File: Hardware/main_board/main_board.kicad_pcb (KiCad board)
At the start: 6 copper layers, 95.4 x 36.1 mm, 282 parts, among them J1 BATT, J2 LCD, J3 BACK_LIGHT, J4 SD, J5 NFC, J6 EXT1, J7 EXT0, J8 USB_C, Q1 DMN313DLT, SW1 OK, SW2 BACK, SW3 RIGHT, SW4 LEFT, SW5 UP, SW6 DOWN, T1 B0310J50100AHF, U1 STM32WB55RGVx, U10 BGS13S4N9E6327XTSA1, U11 NC7SZ32M5X, U12 LP5562TMX, U2 BQ27220YZFR, U3 BQ25896RTWR, U4 RS3221-3.3YF3, U5 LM66100DCK, U6 LM3281YFQR, U7 LM3281YFQR, U8 CC1101RGP, U9 BGS13S4N9E6327XTSA1, Y1 32MHz, Y2 32.768K, Y3 26MHz

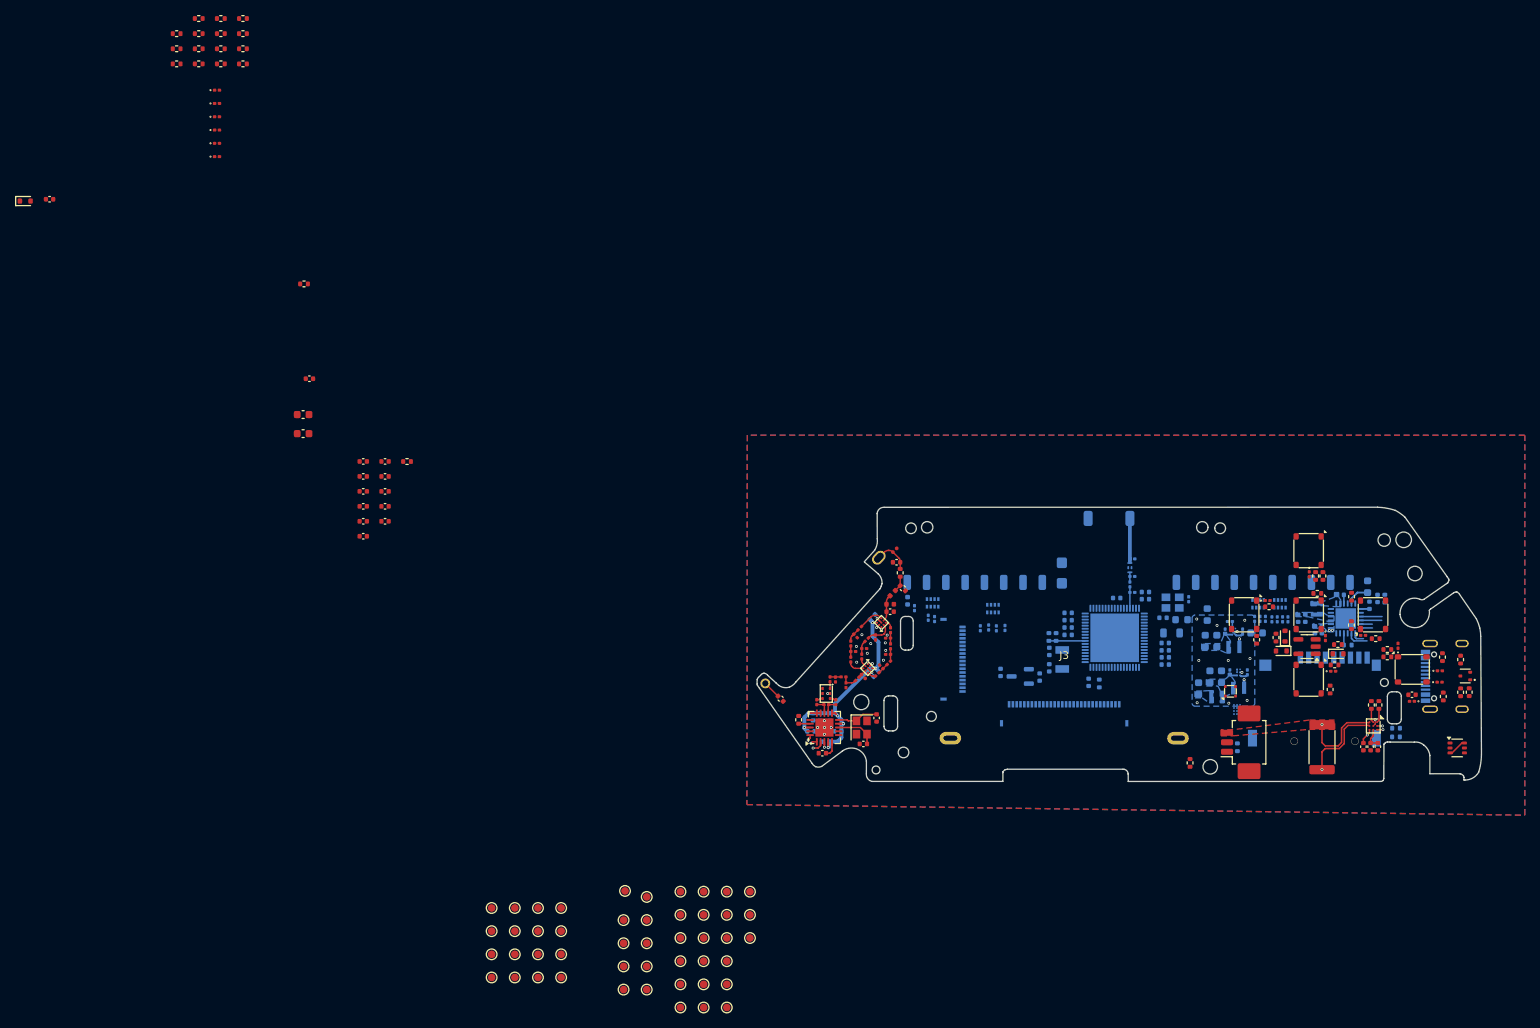
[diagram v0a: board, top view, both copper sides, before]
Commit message: layout: place almost all the components
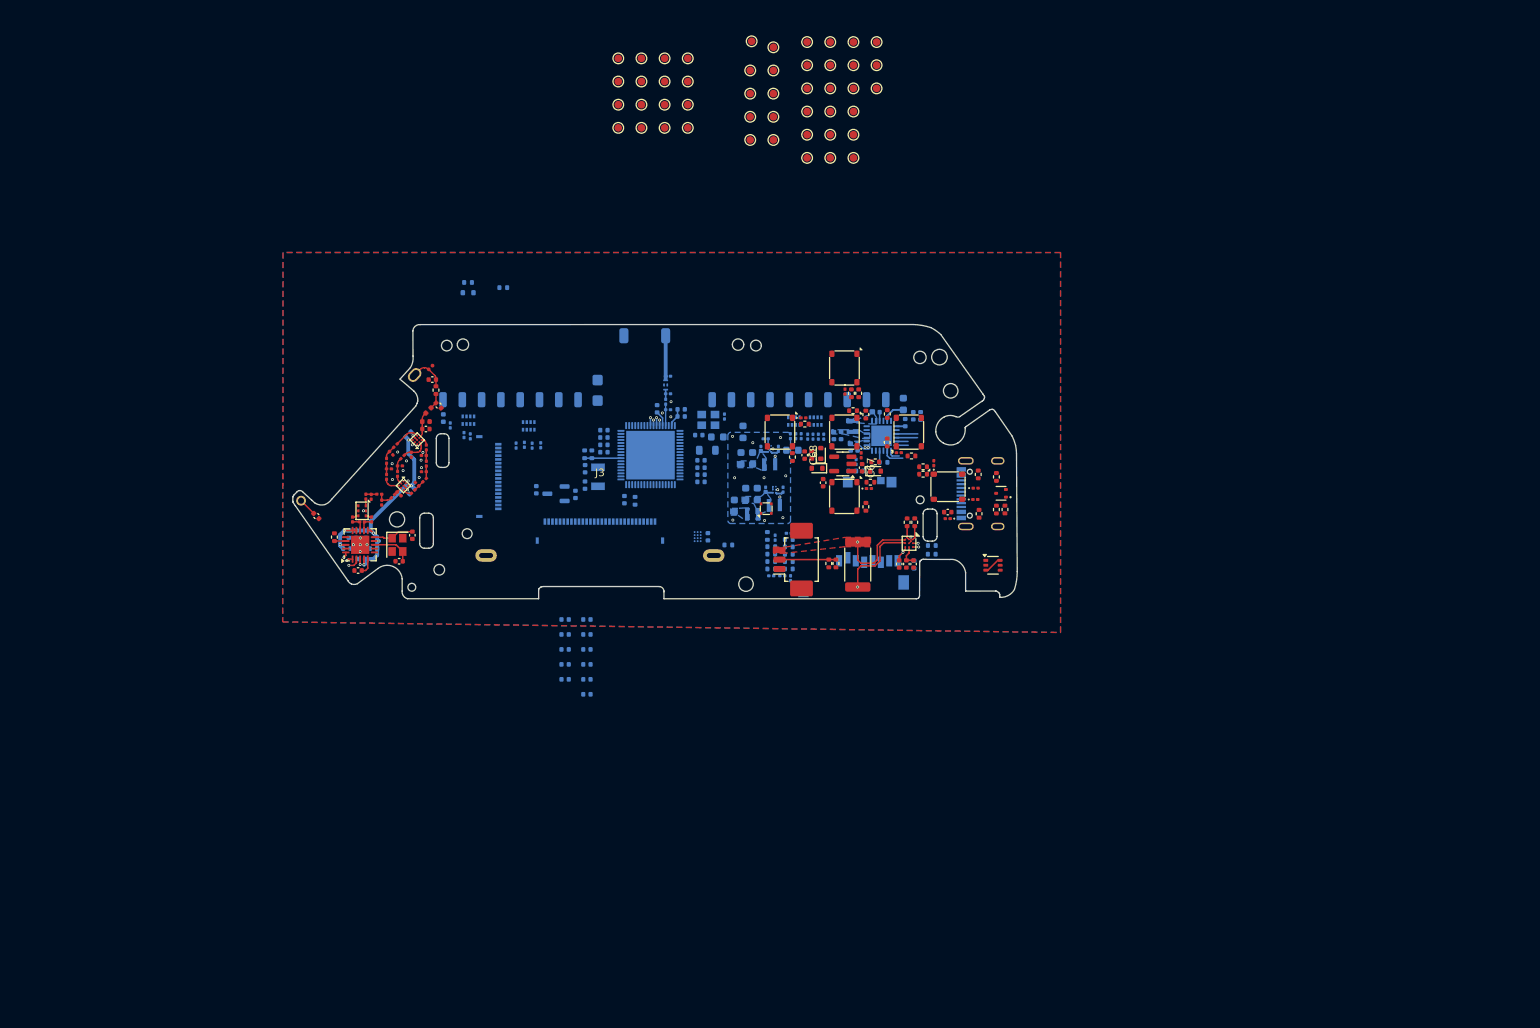
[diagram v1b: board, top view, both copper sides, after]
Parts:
- C67, C68: footprint Capacitor_SMD:C_0603_1608Metric -> Capacitor_SMD:C_0402_1005Metric
- C69, C70, C71, C72, C73, C74, C75, C76, C77, C78, C79, C80, D11, D12, D13, D14, D15, D16, D17, R35, R36, R37, R38, R39, R40, R41, R42, R43, R44, R45, R46, R47, R48, R49, R50: moved to B.Cu
- J4: footprint Library:TF_C393941 -> Library:TF-101A-P3
- R10: moved to F.Cu
- moved R42 115.0 mm to (188.4, 120.5), turned to -90 degrees
- moved TP11 113.1 mm to (174.3, 51.7)
- moved TP13 113.1 mm to (174.3, 57.8)
- moved TP16 113.1 mm to (174.3, 66.9)
- moved TP17 113.1 mm to (177.4, 51.7)
- moved TP19 113.1 mm to (177.4, 57.8)
- moved TP22 113.1 mm to (177.4, 66.9)
- moved TP23 113.1 mm to (180.4, 51.7)
- moved TP25 113.1 mm to (180.4, 57.8)
- moved TP28 113.1 mm to (180.4, 66.9)
- moved TP29 113.1 mm to (183.5, 51.7)
- moved TP31 113.1 mm to (183.5, 57.8)
- moved TP36 113.1 mm to (149.5, 59.9)
- moved TP40 113.1 mm to (152.5, 59.9)
- moved TP44 113.1 mm to (155.6, 59.9)
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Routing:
- net Net-(J1-Pin_2): track 0.00 -> 7.44 mm
- net +3.3V: track 34.6 -> 39.1 mm
- net /MCU/RFID_RF_IN: track 0.00 -> 1.05 mm, vias 0 -> 1
- net /Buttons/BUTTON_UP: track 0.00 -> 1.05 mm, vias 0 -> 1
- net /MCU/PB2: track 0.00 -> 0.74 mm, vias 0 -> 1
- net /Buttons/BUTTON_LEFT: track 0.00 -> 0.74 mm, vias 0 -> 1
- net GND: vias 18 -> 21

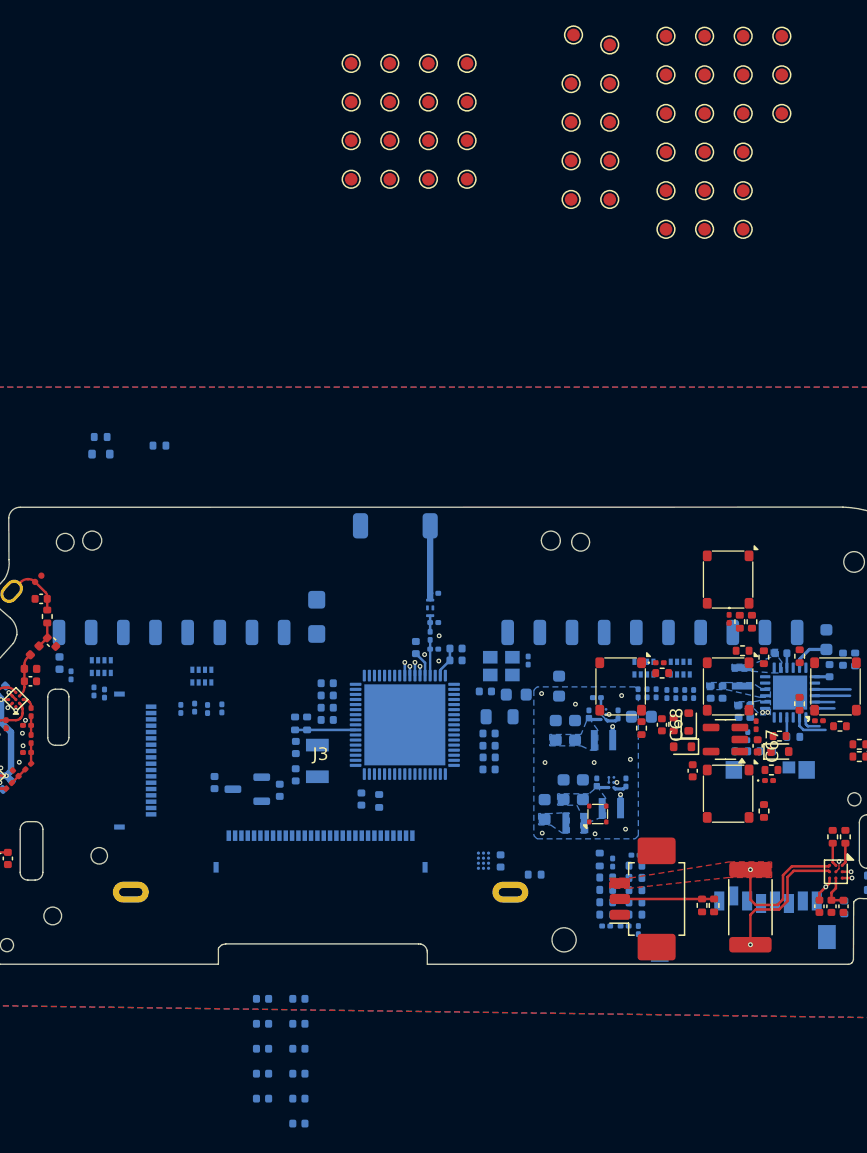
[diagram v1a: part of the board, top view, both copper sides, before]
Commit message: layout: place all the parts
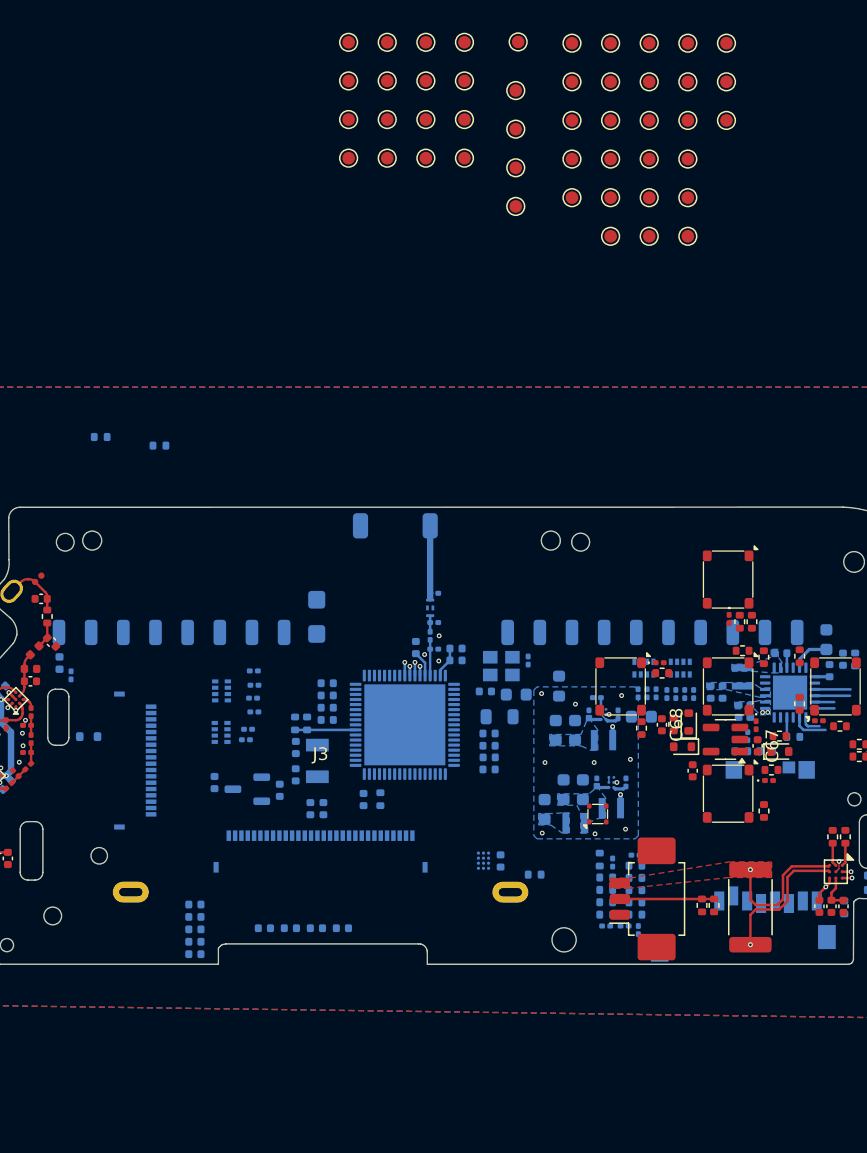
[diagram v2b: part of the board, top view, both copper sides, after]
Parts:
- moved D17 22.3 mm to (128.7, 107.0)
- moved C71 19.0 mm to (146.2, 112.7), turned to -90 degrees
- moved C70 17.1 mm to (147.3, 112.7), turned to -90 degrees
- moved C79 16.2 mm to (137.1, 120.3), turned to 0 degrees
- moved C74 15.7 mm to (142.6, 122.1), turned to 0 degrees
- moved C78 13.5 mm to (137.1, 121.2), turned to 0 degrees
- moved C73 13.5 mm to (144.7, 122.1), turned to 0 degrees
- moved D20 12.6 mm to (141.2, 107.3), turned to 0 degrees
- moved D21 11.7 mm to (141.3, 106.4), turned to 0 degrees
- moved C72 11.6 mm to (146.7, 122.1), turned to 0 degrees
- moved C77 10.8 mm to (137.1, 122.2), turned to 0 degrees
- moved RN1 10.8 mm to (139.2, 106.7), turned to 0 degrees
- moved C76 8.40 mm to (137.1, 123.2), turned to 0 degrees
- moved C69 6.55 mm to (148.8, 122.1), turned to 0 degrees
- moved C75 6.40 mm to (137.1, 124.2), turned to 0 degrees
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
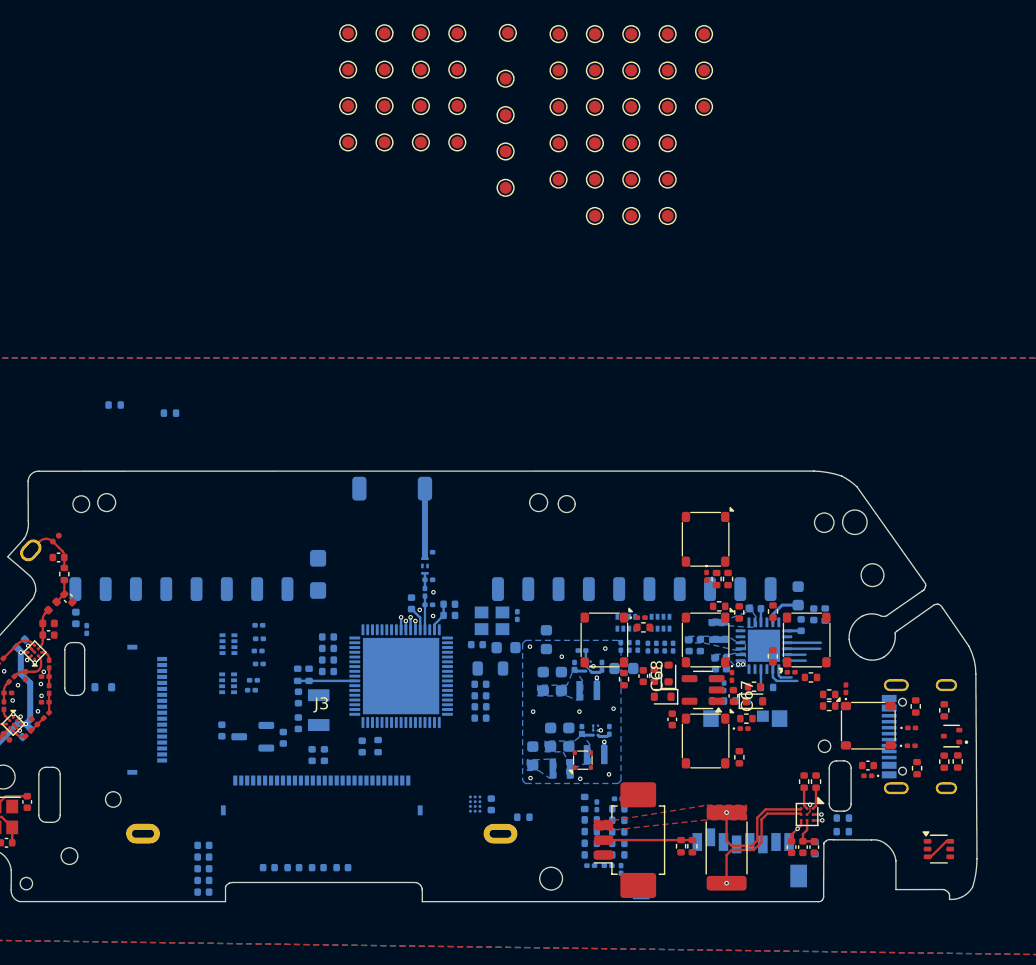
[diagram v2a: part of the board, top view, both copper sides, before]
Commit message: layout: route the power
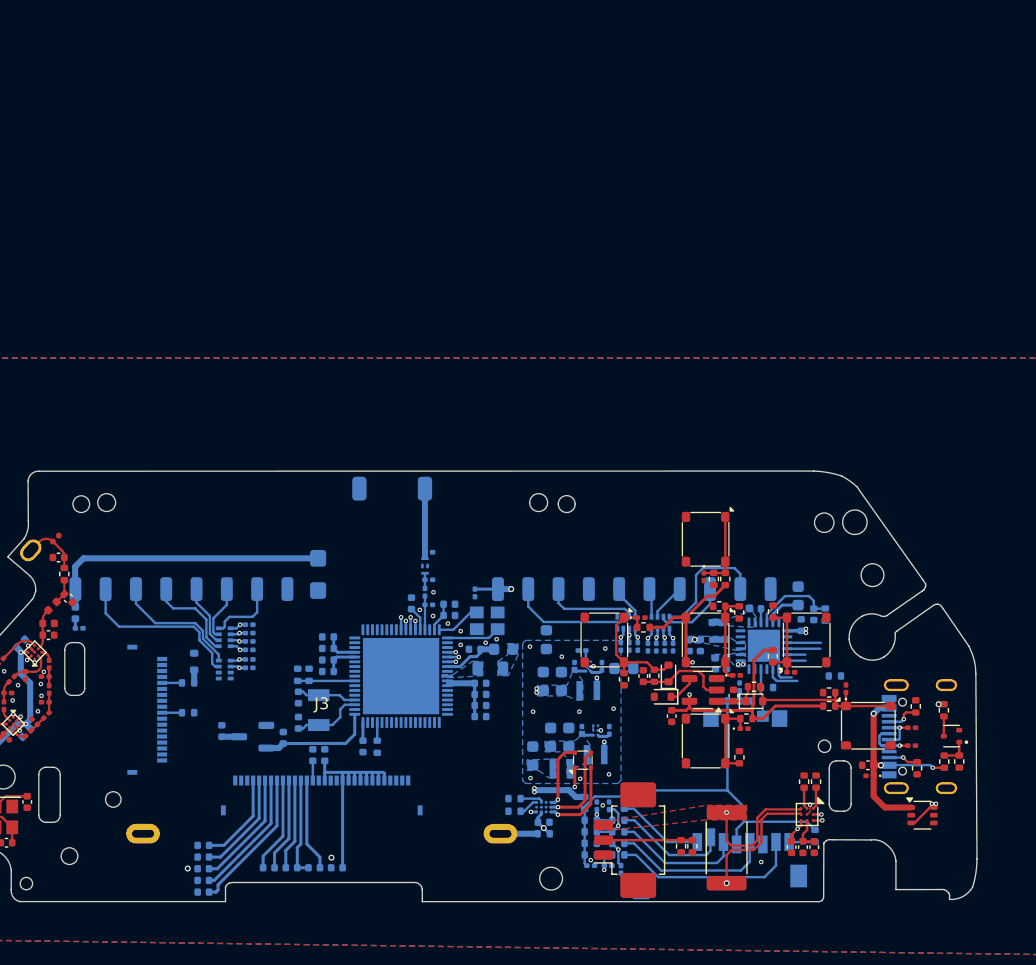
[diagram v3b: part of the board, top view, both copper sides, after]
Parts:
- removed NT1: NetTie, NetTie:NetTie-2_SMD_Pad0.5mm
- removed TP1: RST, TestPoint:TestPoint_Pad_D1.0mm
- removed TP10: D_MOSI, TestPoint:TestPoint_Pad_D1.0mm
- removed TP11: GPOUT, TestPoint:TestPoint_Pad_D1.0mm
- removed TP12, TP13: 5V_USB, TestPoint:TestPoint_Pad_D1.0mm
- removed TP14, TP15: VBAT, TestPoint:TestPoint_Pad_D1.0mm
- removed TP16, TP18: VSYS, TestPoint:TestPoint_Pad_D1.0mm
- removed TP17: STAT, TestPoint:TestPoint_Pad_D1.0mm
- removed TP19: PG, TestPoint:TestPoint_Pad_D1.0mm
- removed TP2: R_SCK, TestPoint:TestPoint_Pad_D1.0mm
- removed TP20: 3V3_MAIN, TestPoint:TestPoint_Pad_D1.0mm
- removed TP21, TP22: 3V3_EXT, TestPoint:TestPoint_Pad_D1.0mm
- removed TP23, TP25: 3V3_LDO, TestPoint:TestPoint_Pad_D1.0mm
- removed TP24: TEMP, TestPoint:TestPoint_Pad_D1.0mm
- removed TP26: PWR_INT, TestPoint:TestPoint_Pad_D1.0mm
- removed TP27, TP28, TP30, TP31: GND, TestPoint:TestPoint_Pad_D1.0mm
- removed TP29: OTG, TestPoint:TestPoint_Pad_D1.0mm
- removed TP3: DM, TestPoint:TestPoint_Pad_D1.0mm
- removed TP34: RFID_C, TestPoint:TestPoint_Pad_D1.0mm
- removed TP35: IR_RX, TestPoint:TestPoint_Pad_D1.0mm
- removed TP36: IR_TX, TestPoint:TestPoint_Pad_D1.0mm
- removed TP37: SP, TestPoint:TestPoint_Pad_D1.0mm
- removed TP38: iBTN, TestPoint:TestPoint_Pad_D1.0mm
- removed TP39: RFID_O, TestPoint:TestPoint_Pad_D1.0mm
- removed TP4: DP, TestPoint:TestPoint_Pad_D1.0mm
- removed TP40: RFID_P, TestPoint:TestPoint_Pad_D1.0mm
- removed TP41: VIBRO, TestPoint:TestPoint_Pad_D1.0mm
- removed TP42: RFID_I, TestPoint:TestPoint_Pad_D1.0mm
- removed TP43: NFC_CS, TestPoint:TestPoint_Pad_D1.0mm
- removed TP44: SWCLK, TestPoint:TestPoint_Pad_D1.0mm
- removed TP45: SWDIO, TestPoint:TestPoint_Pad_D1.0mm
- removed TP46: UART1_TX, TestPoint:TestPoint_Pad_D1.0mm
- removed TP47: UART1_RX, TestPoint:TestPoint_Pad_D1.0mm
- removed TP48: I2C2_SDA, TestPoint:TestPoint_Pad_D1.0mm
- removed TP49: I2C2_SCL, TestPoint:TestPoint_Pad_D1.0mm
- removed TP5: BOOT, TestPoint:TestPoint_Pad_D1.0mm
- removed TP6: D_SCK, TestPoint:TestPoint_Pad_D1.0mm
- removed TP7: D_MISO, TestPoint:TestPoint_Pad_D1.0mm
- removed TP8: R_MISO, TestPoint:TestPoint_Pad_D1.0mm
- removed TP9: R_MOSI, TestPoint:TestPoint_Pad_D1.0mm
- R8: moved to B.Cu
- moved R7 27.7 mm to (163.2, 116.4), turned to 180 degrees
- moved R6 27.5 mm to (163.2, 117.4), turned to 180 degrees
- moved R50 25.2 mm to (135.8, 109.1), turned to 180 degrees
- moved R49 24.1 mm to (135.8, 106.6)
- moved D17 7.92 mm to (136.3, 104.9), turned to 90 degrees
- moved U12 5.75 mm to (165.7, 117.1), turned to 0 degrees
- moved C80 4.65 mm to (165.7, 118.3), turned to 0 degrees
- moved D18 4.03 mm to (159.9, 99.1)
- moved U5 3.16 mm to (197.4, 117.7)
- moved R35 2.20 mm to (165.7, 119.3), turned to 0 degrees
- moved R8 2.01 mm to (190.1, 106.1)
- moved D20 1.89 mm to (141.0, 105.4)
- moved D21 1.79 mm to (141.0, 104.7)
- moved D22 1.46 mm to (141.0, 103.9)
- moved D15 1.30 mm to (182.1, 107.0)
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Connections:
- R5 pad 1: /Power/BAT- -> BAT
- U2 pad C2: /Power/BAT- -> BAT
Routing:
- net +3.3V: track 39.1 -> 105.3 mm, vias 7 -> 9
- net VSYS: track 2.71 -> 56.0 mm, vias 0 -> 4
- net /LCD/LCD_LED: track 0.00 -> 38.7 mm, vias 0 -> 1
- net Net-(D16-A1): track 0.00 -> 36.8 mm
- net BAT: track 0.00 -> 32.6 mm, vias 2 -> 3
- net +3.3V_EXT: track 0.98 -> 29.7 mm, vias 0 -> 5
- net VUSB: track 3.60 -> 27.8 mm, vias 0 -> 4
- net Net-(J7-Pin_1): track 0.00 -> 24.1 mm
- net VBUS: track 0.00 -> 18.3 mm, vias 0 -> 3
- net Net-(J4-DAT0): track 0.00 -> 15.9 mm
- net Net-(J7-Pin_2): track 0.00 -> 14.3 mm
- net /Buttons/BACK: track 0.00 -> 14.2 mm
- net Net-(J4-CLK): track 0.00 -> 13.4 mm
- net Net-(J2-Pin_23): track 0.00 -> 12.1 mm
- net /Buttons/LEFT: track 0.00 -> 11.3 mm
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- added copper zone on B.Cu, net Net-(L1-Pad2)
- added copper zone on B.Cu, net Net-(U1-VLXSMPS)
